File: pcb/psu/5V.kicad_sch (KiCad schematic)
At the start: 18 parts, among them J1 Conn_01x02_Socket, U2 L7815, U3 L7805

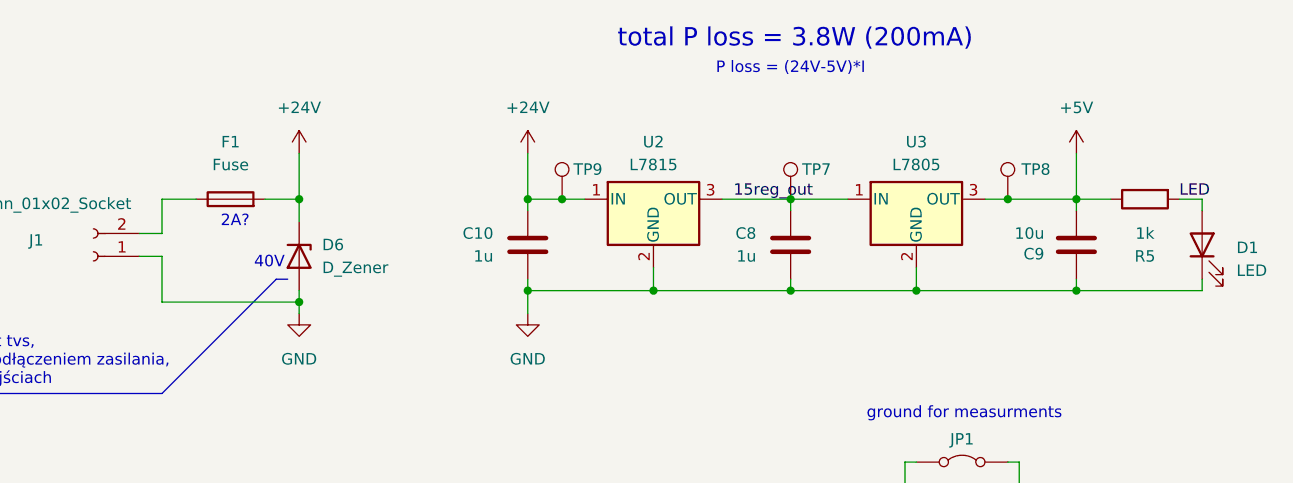
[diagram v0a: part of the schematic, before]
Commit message: poprawki do schematu psu
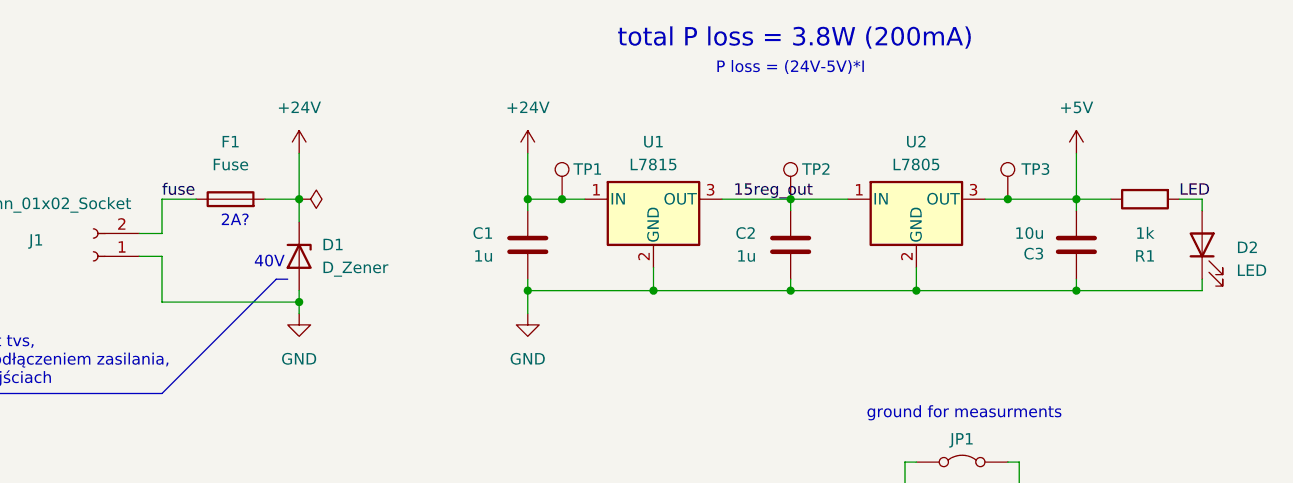
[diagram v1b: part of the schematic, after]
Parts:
- renumbered C10 to C1, C8 to C2, C9 to C3, D6 to D1, D1 to D2, R5 to R1, TP9 to TP1, TP7 to TP2, TP8 to TP3, U2 to U1, U3 to U2
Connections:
- net fuse: now reaches F1.1, J1.2 (Pin_2)
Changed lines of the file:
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@@
+		)
+	)
+	(label "fuse"
+		(at 82.55 95.25 0)
+		(effects
+			(font
+				(size 1.27 1.27)
+			)
+			(justify left bottom)
 		)
 	)
@@
 		(dnp no)
 		(fields_autoplaced yes)
-		(property "Reference" "U2"
+		(property "Reference" "U1"
 			(at 137.16 88.9 0)
 			(effects
@@
 			(project ""
 				(path "/41f68583-7750-4b74-a26b-68c1e6d5dd9b/a0f9a020-68df-4158-8263-f65972a64eca"
-					(reference "U2")
+					(reference "U1")
 					(unit 1)
 				)
@@
 		(on_board yes)
 		(dnp no)
-		(property "Reference" "C8"
+		(property "Reference" "C2"
 			(at 148.59 99.0599 0)
 			(effects
@@
 			(project "Nanopozycjoner_Power_Supply"
 				(path "/41f68583-7750-4b74-a26b-68c1e6d5dd9b/a0f9a020-68df-4158-8263-f65972a64eca"
-					(reference "C8")
+					(reference "C2")
 					(unit 1)
 				)
@@
 		(dnp no)
 		(fields_autoplaced yes)
-		(property "Reference" "D6"
+		(property "Reference" "D1"
 			(at 100.33 100.3299 90)
 			(effects
@@
 			(project ""
 				(path "/41f68583-7750-4b74-a26b-68c1e6d5dd9b/a0f9a020-68df-4158-8263-f65972a64eca"
-					(reference "D6")
+					(reference "D1")
 					(unit 1)
 				)
@@
 		(on_board yes)
 		(dnp no)
-		(property "Reference" "C9"
+		(property "Reference" "C3"
 			(at 180.594 101.346 0)
 			(effects
@@
 			(project "Nanopozycjoner_Power_Supply"
 				(path "/41f68583-7750-4b74-a26b-68c1e6d5dd9b/a0f9a020-68df-4158-8263-f65972a64eca"
-					(reference "C9")
+					(reference "C3")
 					(unit 1)
 				)
@@
 		(on_board yes)
 		(dnp no)
-		(property "Reference" "C10"
+		(property "Reference" "C1"
 			(at 119.38 99.0599 0)
 			(effects
@@
 			(project "Nanopozycjoner_Power_Supply"
 				(path "/41f68583-7750-4b74-a26b-68c1e6d5dd9b/a0f9a020-68df-4158-8263-f65972a64eca"
-					(reference "C10")
+					(reference "C1")
 					(unit 1)
 				)
@@
 		(on_board yes)
 		(dnp no)
-		(property "Reference" "TP7"
+		(property "Reference" "TP2"
 			(at 153.67 91.948 0)
 			(effects
@@
 			(project "Nanopozycjoner_Power_Supply"
 				(path "/41f68583-7750-4b74-a26b-68c1e6d5dd9b/a0f9a020-68df-4158-8263-f65972a64eca"
-					(reference "TP7")
+					(reference "TP2")
 					(unit 1)
 				)
@@
 		(dnp no)
 		(fields_autoplaced yes)
-		(property "Reference" "#PWR010"
+		(property "Reference" "#PWR07"
 			(at 184.15 93.98 0)
 			(effects
@@
 			(project ""
 				(path "/41f68583-7750-4b74-a26b-68c1e6d5dd9b/a0f9a020-68df-4158-8263-f65972a64eca"
-					(reference "#PWR010")
+					(reference "#PWR07")
 					(unit 1)
 				)
@@
 		(dnp no)
 		(fields_autoplaced yes)
-		(property "Reference" "#PWR011"
+		(property "Reference" "#PWR03"
 			(at 123.19 93.98 0)
 			(effects
@@
 			(project "Nanopozycjoner_Power_Supply"
 				(path "/41f68583-7750-4b74-a26b-68c1e6d5dd9b/a0f9a020-68df-4158-8263-f65972a64eca"
-					(reference "#PWR011")
+					(reference "#PWR03")
 					(unit 1)
 				)
@@
 		(dnp no)
 		(fields_autoplaced yes)
-		(property "Reference" "#PWR030"
+		(property "Reference" "#PWR05"
 			(at 165.1 133.35 0)
 			(effects
@@
 			(project "Nanopozycjoner_Power_Supply"
 				(path "/41f68583-7750-4b74-a26b-68c1e6d5dd9b/a0f9a020-68df-4158-8263-f65972a64eca"
-					(reference "#PWR030")
+					(reference "#PWR05")
+					(unit 1)
+				)
+			)
+		)
+	)
+	(symbol
+		(lib_id "power:PWR_FLAG")
+		(at 97.79 95.25 270)
+		(unit 1)
+		(exclude_from_sim no)
+		(in_bom yes)
+		(on_board yes)
+		(dnp no)
+		(fields_autoplaced yes)
+		(property "Reference" "#FLG05"
+			(at 99.695 95.25 0)
+			(effects
+				(font
+					(size 1.27 1.27)
+				)
+				(hide yes)
+			)
+		)
+		(property "Value" "PWR_FLAG"
+			(at 102.87 95.25 0)
+			(effects
+				(font
+					(size 1.27 1.27)
+				)
+				(hide yes)
+			)
+		)
+		(property "Footprint" ""
+			(at 97.79 95.25 0)
+			(effects
+				(font
+					(size 1.27 1.27)
+				)
+				(hide yes)
+			)
+		)
+		(property "Datasheet" "~"
+			(at 97.79 95.25 0)
+			(effects
+				(font
+					(size 1.27 1.27)
+				)
+				(hide yes)
+			)
+		)
+		(property "Description" "Special symbol for telling ERC where power comes from"
+			(at 97.79 95.25 0)
+			(effects
+				(font
+					(size 1.27 1.27)
+				)
+				(hide yes)
+			)
+		)
+		(pin "1"
+		)
+		(instances
+			(project "Nanopozycjoner_Power_Supply"
+				(path "/41f68583-7750-4b74-a26b-68c1e6d5dd9b/a0f9a020-68df-4158-8263-f65972a64eca"
+					(reference "#FLG05")
 					(unit 1)
 				)
@@
 		(dnp no)
 		(fields_autoplaced yes)
-		(property "Reference" "U3"
+		(property "Reference" "U2"
 			(at 166.37 88.9 0)
 			(effects
@@
 			(project ""
 				(path "/41f68583-7750-4b74-a26b-68c1e6d5dd9b/a0f9a020-68df-4158-8263-f65972a64eca"
-					(reference "U3")
+					(reference "U2")
 					(unit 1)
 				)
@@
 		(on_board yes)
 		(dnp no)
-		(property "Reference" "R5"
+		(property "Reference" "R1"
 			(at 191.77 101.6 90)
 			(effects
@@
 			(project ""
 				(path "/41f68583-7750-4b74-a26b-68c1e6d5dd9b/a0f9a020-68df-4158-8263-f65972a64eca"
-					(reference "R5")
+					(reference "R1")
 					(unit 1)
 				)
@@
 		(dnp no)
 		(fields_autoplaced yes)
-		(property "Reference" "#PWR031"
+		(property "Reference" "#PWR06"
 			(at 177.8 133.35 0)
 			(effects
@@
 			(project "Nanopozycjoner_Power_Supply"
 				(path "/41f68583-7750-4b74-a26b-68c1e6d5dd9b/a0f9a020-68df-4158-8263-f65972a64eca"
-					(reference "#PWR031")
+					(reference "#PWR06")
 					(unit 1)
 				)
@@
 		(dnp no)
 		(fields_autoplaced yes)
-		(property "Reference" "D1"
+		(property "Reference" "D2"
 			(at 201.93 100.6474 90)
 			(effects
@@
 			(project ""
 				(path "/41f68583-7750-4b74-a26b-68c1e6d5dd9b/a0f9a020-68df-4158-8263-f65972a64eca"
-					(reference "D1")
+					(reference "D2")
 					(unit 1)
 				)
@@
 		(dnp no)
 		(fields_autoplaced yes)
-		(property "Reference" "#PWR015"
+		(property "Reference" "#PWR01"
 			(at 97.79 93.98 0)
 			(effects
@@
 			(project "Nanopozycjoner_Power_Supply"
 				(path "/41f68583-7750-4b74-a26b-68c1e6d5dd9b/a0f9a020-68df-4158-8263-f65972a64eca"
-					(reference "#PWR015")
+					(reference "#PWR01")
 					(unit 1)
 				)
@@
 		(on_board yes)
 		(dnp no)
-		(property "Reference" "TP9"
+		(property "Reference" "TP1"
 			(at 128.27 91.948 0)
 			(effects
@@
 			(project "Nanopozycjoner_Power_Supply"
 				(path "/41f68583-7750-4b74-a26b-68c1e6d5dd9b/a0f9a020-68df-4158-8263-f65972a64eca"
-					(reference "TP9")
+					(reference "TP1")
 					(unit 1)
 				)
@@
 		(dnp no)
 		(fields_autoplaced yes)
-		(property "Reference" "#PWR07"
+		(property "Reference" "#PWR04"
 			(at 123.19 114.3 0)
 			(effects
@@
 			(project ""
 				(path "/41f68583-7750-4b74-a26b-68c1e6d5dd9b/a0f9a020-68df-4158-8263-f65972a64eca"
-					(reference "#PWR07")
+					(reference "#PWR04")
 					(unit 1)
 				)
@@
 		(dnp no)
 		(fields_autoplaced yes)
-		(property "Reference" "#PWR016"
+		(property "Reference" "#PWR02"
 			(at 97.79 114.3 0)
 			(effects
@@
 			(project "Nanopozycjoner_Power_Supply"
 				(path "/41f68583-7750-4b74-a26b-68c1e6d5dd9b/a0f9a020-68df-4158-8263-f65972a64eca"
-					(reference "#PWR016")
+					(reference "#PWR02")
 					(unit 1)
 				)
@@
 		(on_board yes)
 		(dnp no)
-		(property "Reference" "TP8"
+		(property "Reference" "TP3"
 			(at 178.054 91.948 0)
 			(effects
@@
 			(project "Nanopozycjoner_Power_Supply"
 				(path "/41f68583-7750-4b74-a26b-68c1e6d5dd9b/a0f9a020-68df-4158-8263-f65972a64eca"
-					(reference "TP8")
-					(unit 1)
-				)
+					(reference "TP3")
+					(unit 1)
+				)

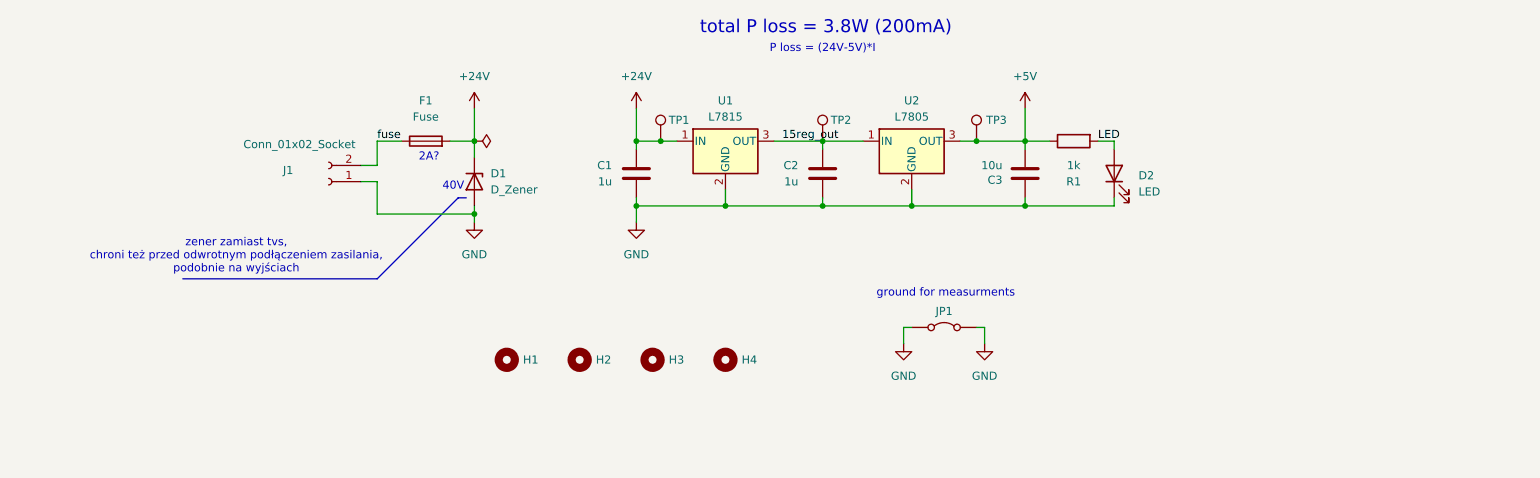
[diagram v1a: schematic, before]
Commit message: added PSU PCB design files
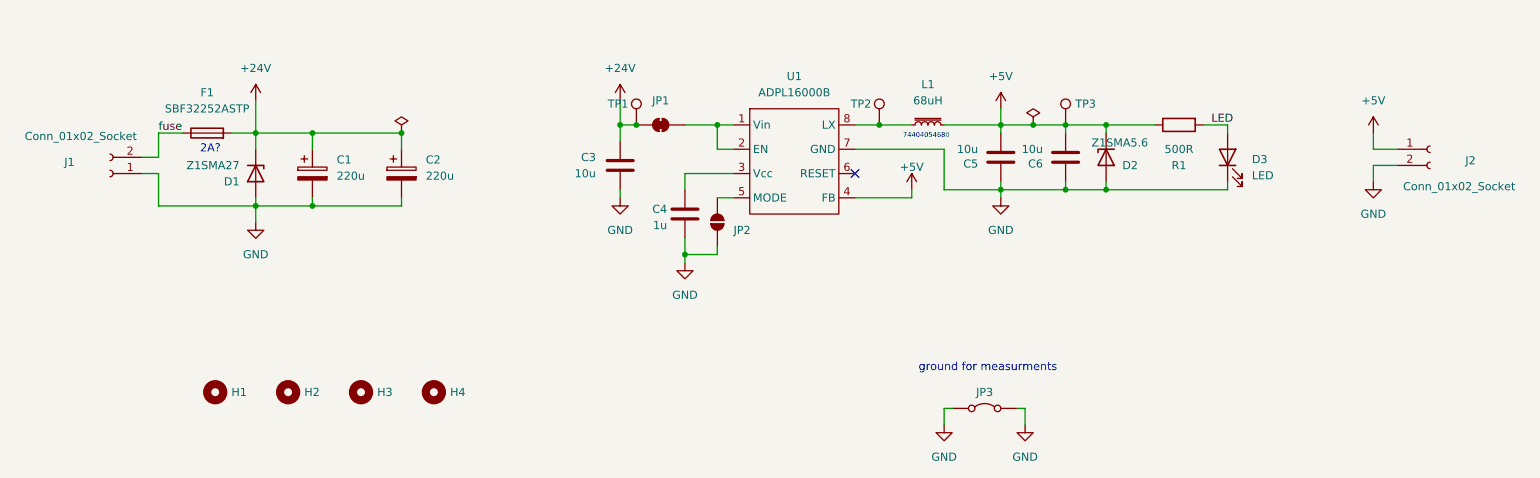
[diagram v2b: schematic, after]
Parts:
- removed C1, C2: 1u, symbol Device:C
- removed D1: D_Zener, symbol Device:D_Zener
- removed U1: L7815, symbol Regulator_Linear:L7815
- removed U2: L7805, symbol Regulator_Linear:L7805
- added C1, C2: 220u, Capacitor_THT:CP_Radial_D8.0mm_P3.50mm, symbol Device:C_Polarized
- added C4: 1u, Capacitor_SMD:C_0805_2012Metric, symbol Device:C
- added C5, C6: 10u, Capacitor_SMD:C_0805_2012Metric, symbol Device:C
- added D1: Z1SMA27, Diode_SMD:D_SMA, symbol Diode:Z1SMAxxx
- added D2: Z1SMA5.6, Diode_SMD:D_SMA, symbol Diode:Z1SMAxxx
- added J2: Conn_01x02_Socket, Connector_Wago:Wago_734-132_1x02_P3.50mm_Vertical, symbol Connector:Conn_01x02_Socket
- added JP1: SolderJumper_2_Bridged, Jumper:SolderJumper-2_P1.3mm_Bridged2Bar_RoundedPad1.0x1.5mm, symbol Jumper:SolderJumper_2_Bridged
- added JP2: SolderJumper_2_Open, Jumper:SolderJumper-2_P1.3mm_Bridged_RoundedPad1.0x1.5mm, symbol Jumper:SolderJumper_2_Open
- added L1: 68uH, Inductor_SMD:L_Wuerth_MAPI-5030, symbol Device:L_Iron_Small
- added U1: ADPL16000B, Library:ADPL16000footprint, symbol New_Library:ADPL16000
- C3: footprint (none) -> Capacitor_SMD:C_0805_2012Metric
- D3: renamed from D2; footprint (none) -> LED_SMD:LED_0603_1608Metric
- F1: value Fuse -> SBF32252ASTP; footprint (none) -> Fuse:Fuse_1206_3216Metric
- H1, H2, H3, H4: footprint (none) -> MountingHole:MountingHole_4.3mm_M4_ISO14580
- J1: footprint (none) -> Connector_Wago:Wago_734-132_1x02_P3.50mm_Vertical
- JP3: renamed from JP1; footprint (none) -> Capacitor_THT:C_Axial_L12.0mm_D6.5mm_P20.00mm_Horizontal
- R1: value 1k -> 500R; footprint (none) -> Resistor_SMD:R_0805_2012Metric
- TP1, TP2, TP3: footprint (none) -> TestPoint:TestPoint_Pad_D1.5mm
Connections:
- net +24V: now also C3.1, C1.1, C2.1, D1.1 (K), JP1.1 (A)
- net +5V: now also C5.2, C6.2, D2.1 (K), J2.1 (Pin_1), L1.2, U1.4 (FB); no longer C3.2
- net GND: now also C3.2, C1.2, C2.2, C4.2, C5.1, C6.1, D1.2 (A), D2.2 (A), J2.2 (Pin_2), JP2.1 (A), U1.7 (GND); no longer C3.1
- net 15reg_out: no longer names the net of TP2.1
- net 15reg_out: now also L1.1, U1.8 (LX)
- new net: JP1.2 (B), U1.1 (Vin), U1.2 (EN)
- new net: C4.1, U1.3 (Vcc)
- new net: JP2.2 (B), U1.5 (MODE)
- no-connect marks 0 -> 1
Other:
- note added: "74404054680"
- note removed: "40V"
- note removed: "P loss = (24V-5V)*I"
- note removed: "total P loss = 3.8W (200mA)"
- note removed: "zener zamiast tvs, chroni też przed odwrotnym podłączeniem zasilania, podobnie na wyjściach"
- moved on the sheet: D3, F1, H1, H2, H3, H4, J1, JP3, R1, TP3

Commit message: final changes
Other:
- moved on the sheet: C1, C2, D1, F1, H1, H2, H3, H4, J1, J2, JP1, JP3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
